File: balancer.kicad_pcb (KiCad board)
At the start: 2 copper layers, 50 x 50 mm, 53 parts, among them IC1 TLV3404, IC2 MAX923, IC3 MAX923, IC4 MAX923, J1 S4B-XH-SM4-TB, J2 Output (+), J3 Output (-), J4 Input (+), J5 Input (-), Q1 IRF7455PBF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

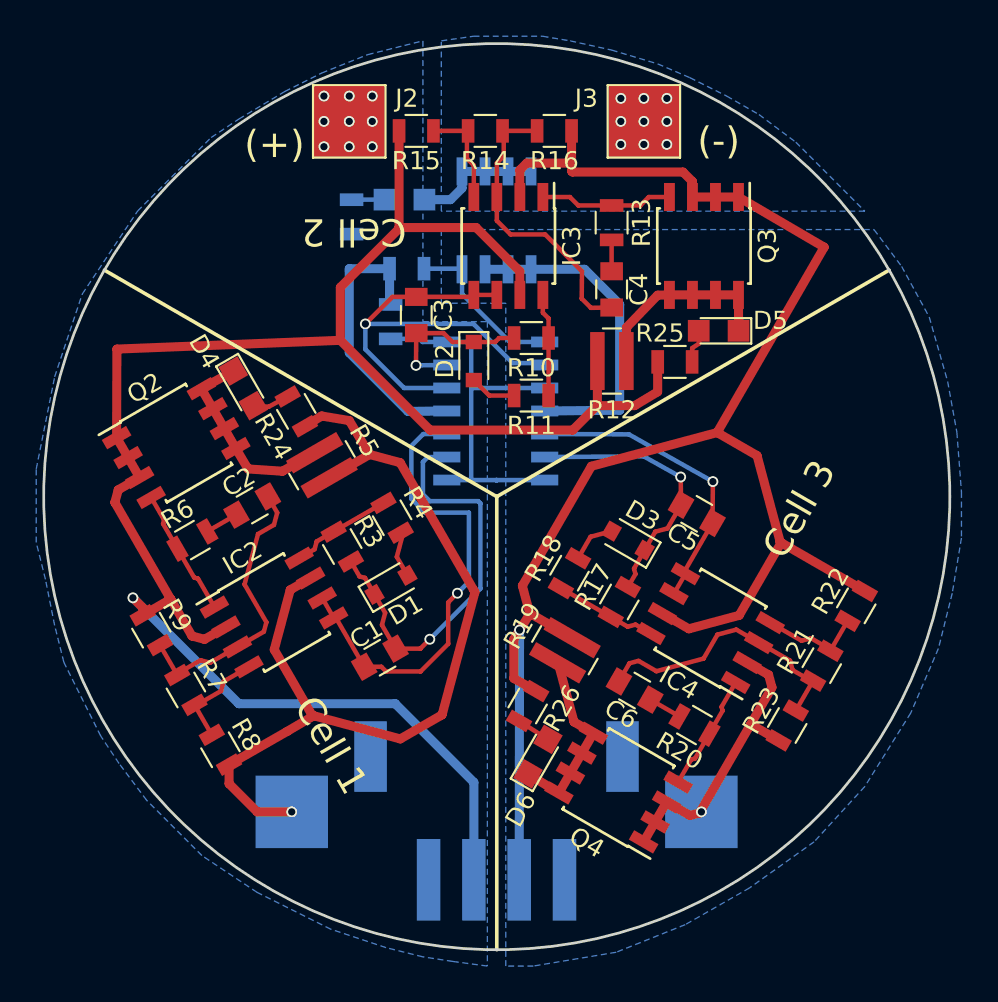
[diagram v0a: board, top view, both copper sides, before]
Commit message: added missing 3d models, recreated gerbers and drill files
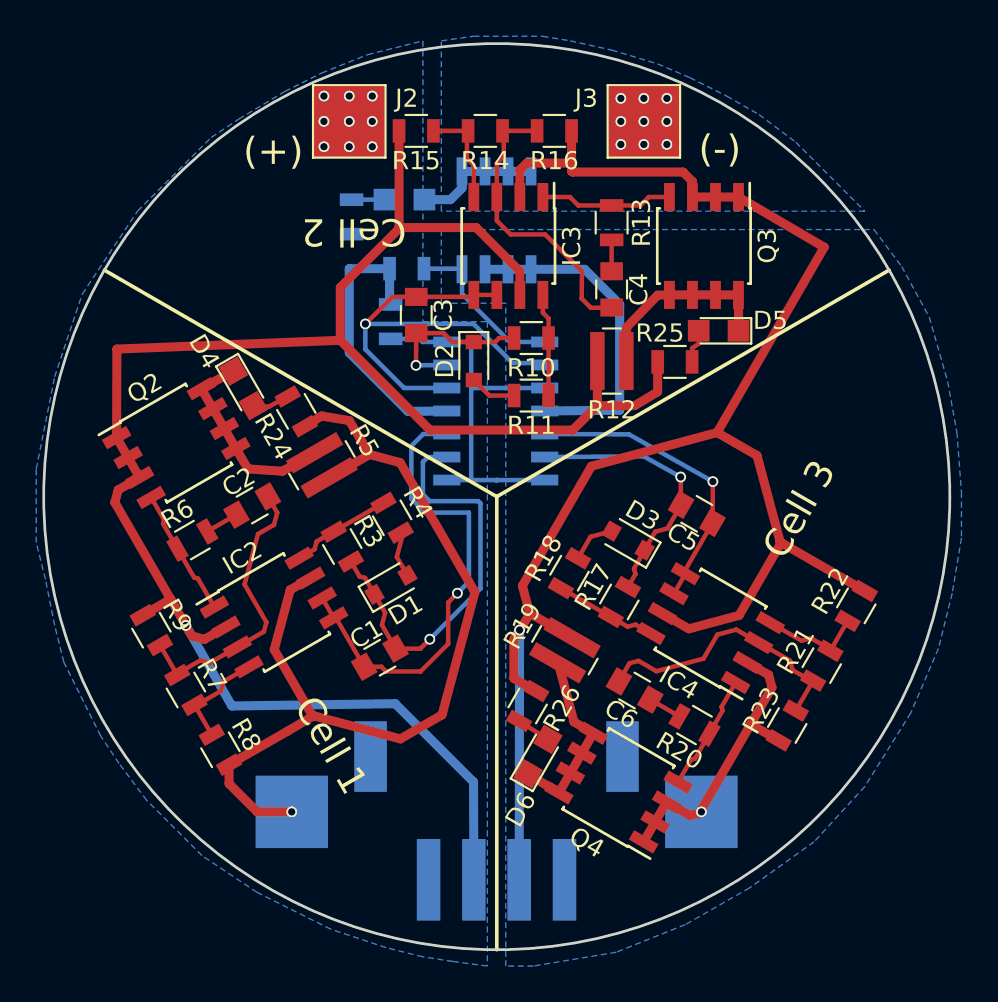
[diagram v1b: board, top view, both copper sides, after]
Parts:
- D1, D2, D3: footprint Diodes_SMD:D_0805 -> balancer:D_0805
- R12, R19, R5: footprint Resistors_SMD:R_0612 -> balancer:R_0612
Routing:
- net /Cell2+: track 110.2 -> 106.2 mm
